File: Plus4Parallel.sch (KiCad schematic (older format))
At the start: 3 parts, among them CN1 PLUS4_USERPORT, J1 DB25_Female_MountingHoles

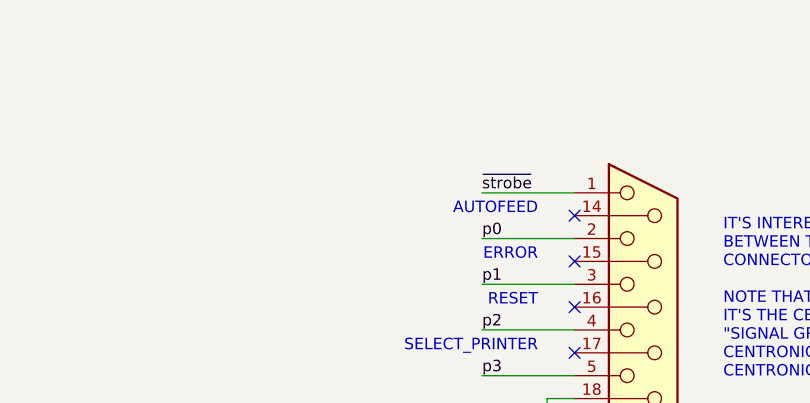
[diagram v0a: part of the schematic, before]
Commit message: Add power jumper Inspired by Amiga
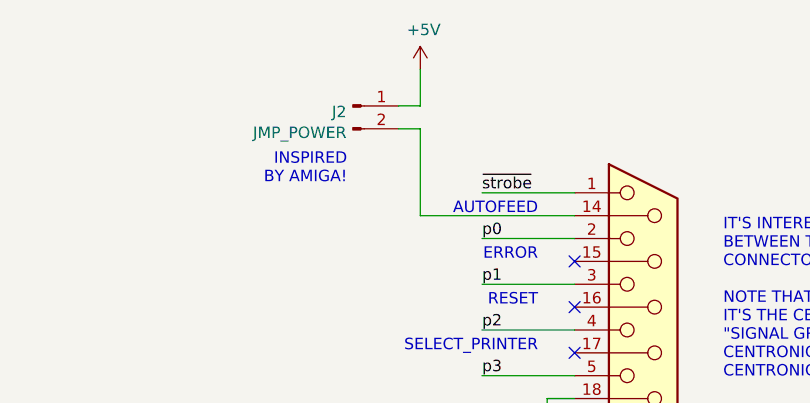
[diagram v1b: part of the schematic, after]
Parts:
- added J2: JMP_POWER, Connector_PinHeader_2.54mm:PinHeader_1x02_P2.54mm_Vertical, symbol Connector:Conn_01x02_Male
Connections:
- net +5V: now also J2.1 (Pin_1)
- net at J1.14 (P14): now also J2.2 (Pin_2)
- no-connect marks 16 -> 15
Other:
- note added: "INSPIRED\nBY AMIGA!"
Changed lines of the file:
@@
 NoConn ~ 7840 4115
 NoConn ~ 7840 3015
-NoConn ~ 7840 2415
 NoConn ~ 7840 2615
 Text Notes 7680 2615 2    50   ~ 0
@@
 SELECT_PRINTER
 NoConn ~ 7840 2815
-Wire Bus Line
-	2420 3165 2420 4570
-Wire Bus Line
-	4745 2965 4745 4570
 Text Notes 7680 2815 2    50   ~ 0
 RESET
@@
 	1    0    0    -1
 $EndComp
+Wire Wire Line
+	7840 2415 7165 2415
+Wire Wire Line
+	7165 2415 7165 2035
+$Comp
+L Connector:Conn_01x02_Male J2
+U 1 1 650B3912
+P 6870 1935
+F 0 "J2" H 6842 1909 50  0000 R CNN
+F 1 "JMP_POWER" H 6842 1818 50  0000 R CNN
+F 2 "Connector_PinHeader_2.54mm:PinHeader_1x02_P2.54mm_Vertical" H 6870 1935 50  0001 C CNN
+F 3 "~" H 6870 1935 50  0001 C CNN
+	1    6870 1935
+	1    0    0    -1
+$EndComp
+Wire Wire Line
+	7165 1935 7165 1775
+$Comp
+L power:+5V #PWR04
+U 1 1 650B505F
+P 7165 1775
+F 0 "#PWR04" H 7165 1625 50  0001 C CNN
+F 1 "+5V" H 7180 1948 50  0000 C CNN
+F 2 "" H 7165 1775 50  0001 C CNN
+F 3 "" H 7165 1775 50  0001 C CNN
+	1    7165 1775
+	1    0    0    -1
+$EndComp
+Wire Wire Line
+	7070 1935 7165 1935
+Wire Wire Line
+	7070 2035 7165 2035
+Wire Bus Line
+	2420 3165 2420 4570
+Wire Bus Line
+	4745 2965 4745 4570
+Text Notes 6845 2280 2    50   ~ 0
+INSPIRED\nBY AMIGA!
 $EndSCHEMATC
